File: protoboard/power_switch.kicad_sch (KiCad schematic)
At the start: 15 parts, among them IC1 TMCS1123B1AQDVGR, IC2 LTC7067RMSE#PBF, IC3 LTC7067RMSE#PBF, J3 Conn_01x02_Socket, J4 Conn_01x02_Socket, Q1 NMOS, Q2 NMOS, Q3 NMOS, Q4 NMOS

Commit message: finish protoboard v1
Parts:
- IC1: footprint TMCS1123B1AQDVGR -> libs:TMCS1123B1AQDVGR
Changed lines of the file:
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@@
+	)
+	(junction
+		(at 34.29 43.18)
+		(diameter 0)
+		(color 0 0 0 0)
 	)
 	(junction
@@
 	(wire
 		(pts
+			(xy 34.29 43.18) (xy 34.29 41.91)
+		)
+		(stroke
+			(width 0)
+			(type default)
+		)
+	)
+	(wire
+		(pts
 			(xy 139.7 41.91) (xy 139.7 64.77)
 		)
@@
 	(wire
 		(pts
-			(xy 34.29 45.72) (xy 34.29 41.91)
+			(xy 34.29 45.72) (xy 34.29 43.18)
 		)
 		(stroke
@@
 			)
 		)
-		(property "Footprint" "TMCS1123B1AQDVGR"
+		(property "Footprint" "libs:TMCS1123B1AQDVGR"
 			(at 146.05 242.24 0)
 			(effects
@@
 					(unit 1)
 				)
+			)
+		)
+	)
+	(symbol
+		(lib_id "power:PWR_FLAG")
+		(at 34.29 43.18 90)
+		(unit 1)
+		(exclude_from_sim no)
+		(in_bom yes)
+		(on_board yes)
+		(dnp no)
+		(fields_autoplaced yes)
+		(property "Reference" "#FLG03"
+			(at 32.385 43.18 0)
+			(effects
+				(font
+					(size 1.27 1.27)
+				)
+				(hide yes)
+			)
+		)
+		(property "Value" "PWR_FLAG"
+			(at 30.48 43.1799 90)
+			(effects
+				(font
+					(size 1.27 1.27)
+				)
+				(justify left)
+			)
+		)
+		(property "Footprint" ""
+			(at 34.29 43.18 0)
+			(effects
+				(font
+					(size 1.27 1.27)
+				)
+				(hide yes)
+			)
+		)
+		(property "Datasheet" "~"
+			(at 34.29 43.18 0)
+			(effects
+				(font
+					(size 1.27 1.27)
+				)
+				(hide yes)
+			)
+		)
+		(property "Description" "Special symbol for telling ERC where power comes from"
+			(at 34.29 43.18 0)
+			(effects
+				(font
+					(size 1.27 1.27)
+				)
+				(hide yes)
+			)
+		)
+		(pin "1"
+		)
+		(instances
+			(project ""
+				(path "/9233c06e-90cd-4cc2-bc77-fac00ef686c2/7cfc6854-4f26-43a9-ad66-98f80f8ef6d6"
+					(reference "#FLG03")
+					(unit 1)
+				)

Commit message: footprint update
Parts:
- C1, C2, C3: footprint (none) -> Capacitor_SMD:C_0603_1608Metric_Pad1.08x0.95mm_HandSolder
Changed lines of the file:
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@@
 			)
 		)
-		(property "Footprint" ""
+		(property "Footprint" "Capacitor_SMD:C_0603_1608Metric_Pad1.08x0.95mm_HandSolder"
 			(at 140.6652 73.66 0)
 			(effects
@@
 			)
 		)
-		(property "Footprint" ""
+		(property "Footprint" "Capacitor_SMD:C_0603_1608Metric_Pad1.08x0.95mm_HandSolder"
 			(at 204.1652 72.39 0)
 			(effects
@@
 			)
 		)
-		(property "Footprint" ""
+		(property "Footprint" "Capacitor_SMD:C_0603_1608Metric_Pad1.08x0.95mm_HandSolder"
 			(at 72.39 140.97 0)
 			(effects

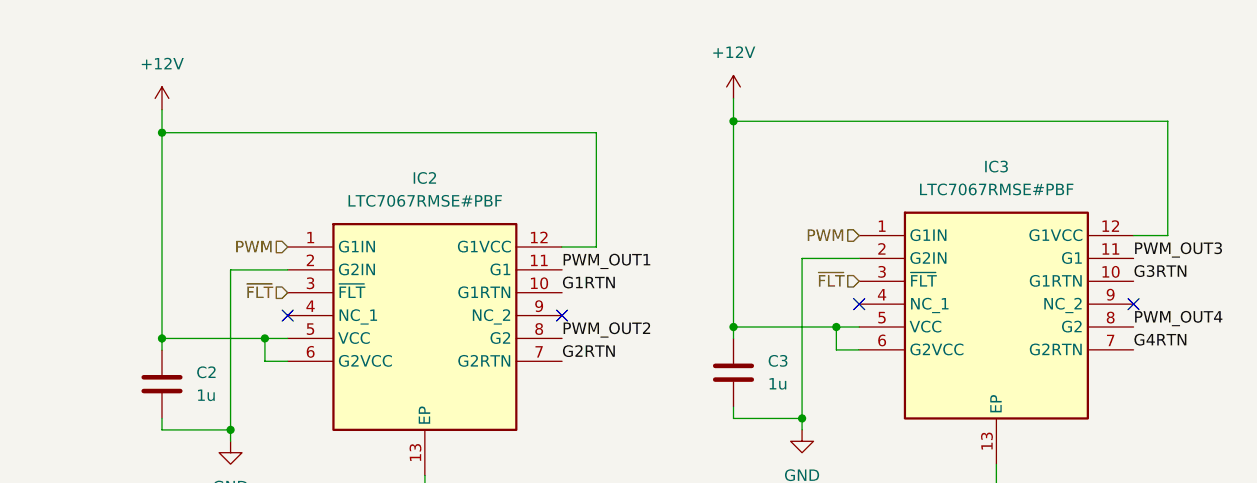
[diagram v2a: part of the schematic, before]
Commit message: schematic review changes
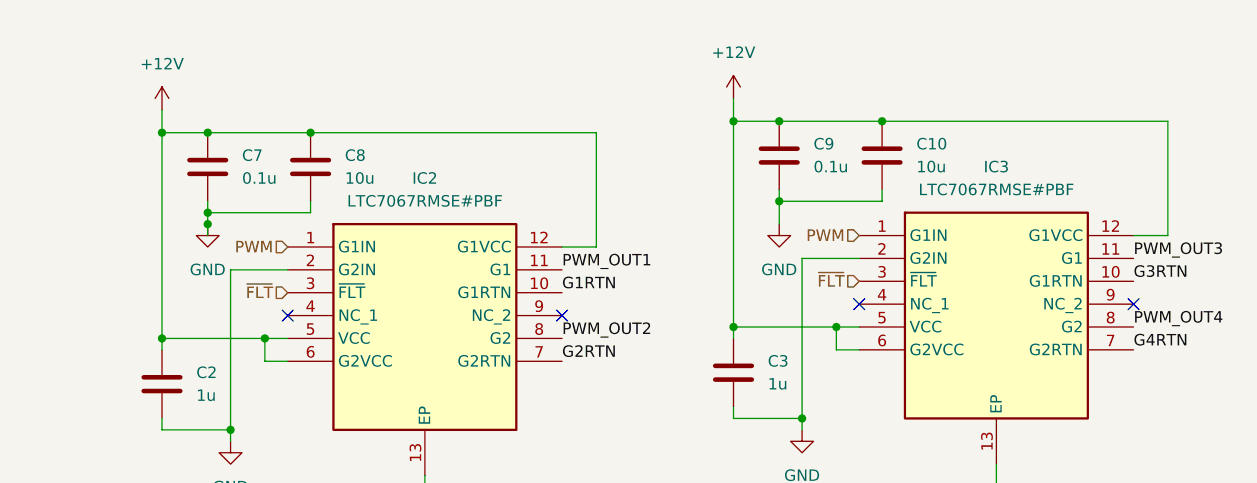
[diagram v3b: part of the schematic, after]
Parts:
- added C10, C8: 10u, Capacitor_SMD:C_0603_1608Metric, symbol Device:C
- added C7, C9: 0.1u, Capacitor_SMD:C_0603_1608Metric, symbol Device:C
- C1: footprint Capacitor_SMD:C_0603_1608Metric_Pad1.08x0.95mm_HandSolder -> Capacitor_THT:CP_Radial_D16.0mm_P7.50mm
- D1, D2: footprint (none) -> Package_TO_SOT_THT:TO-247-3_Vertical
- IC2, IC3: footprint SOP65P490X110-13N -> libs:05-08-1666_ADI
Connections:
- net +12V: now also C10.1, C7.1, C8.1, C9.1
- net GND: now also C10.2, C7.2, C8.2, C9.2
